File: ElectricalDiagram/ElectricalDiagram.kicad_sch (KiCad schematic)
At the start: 29 parts

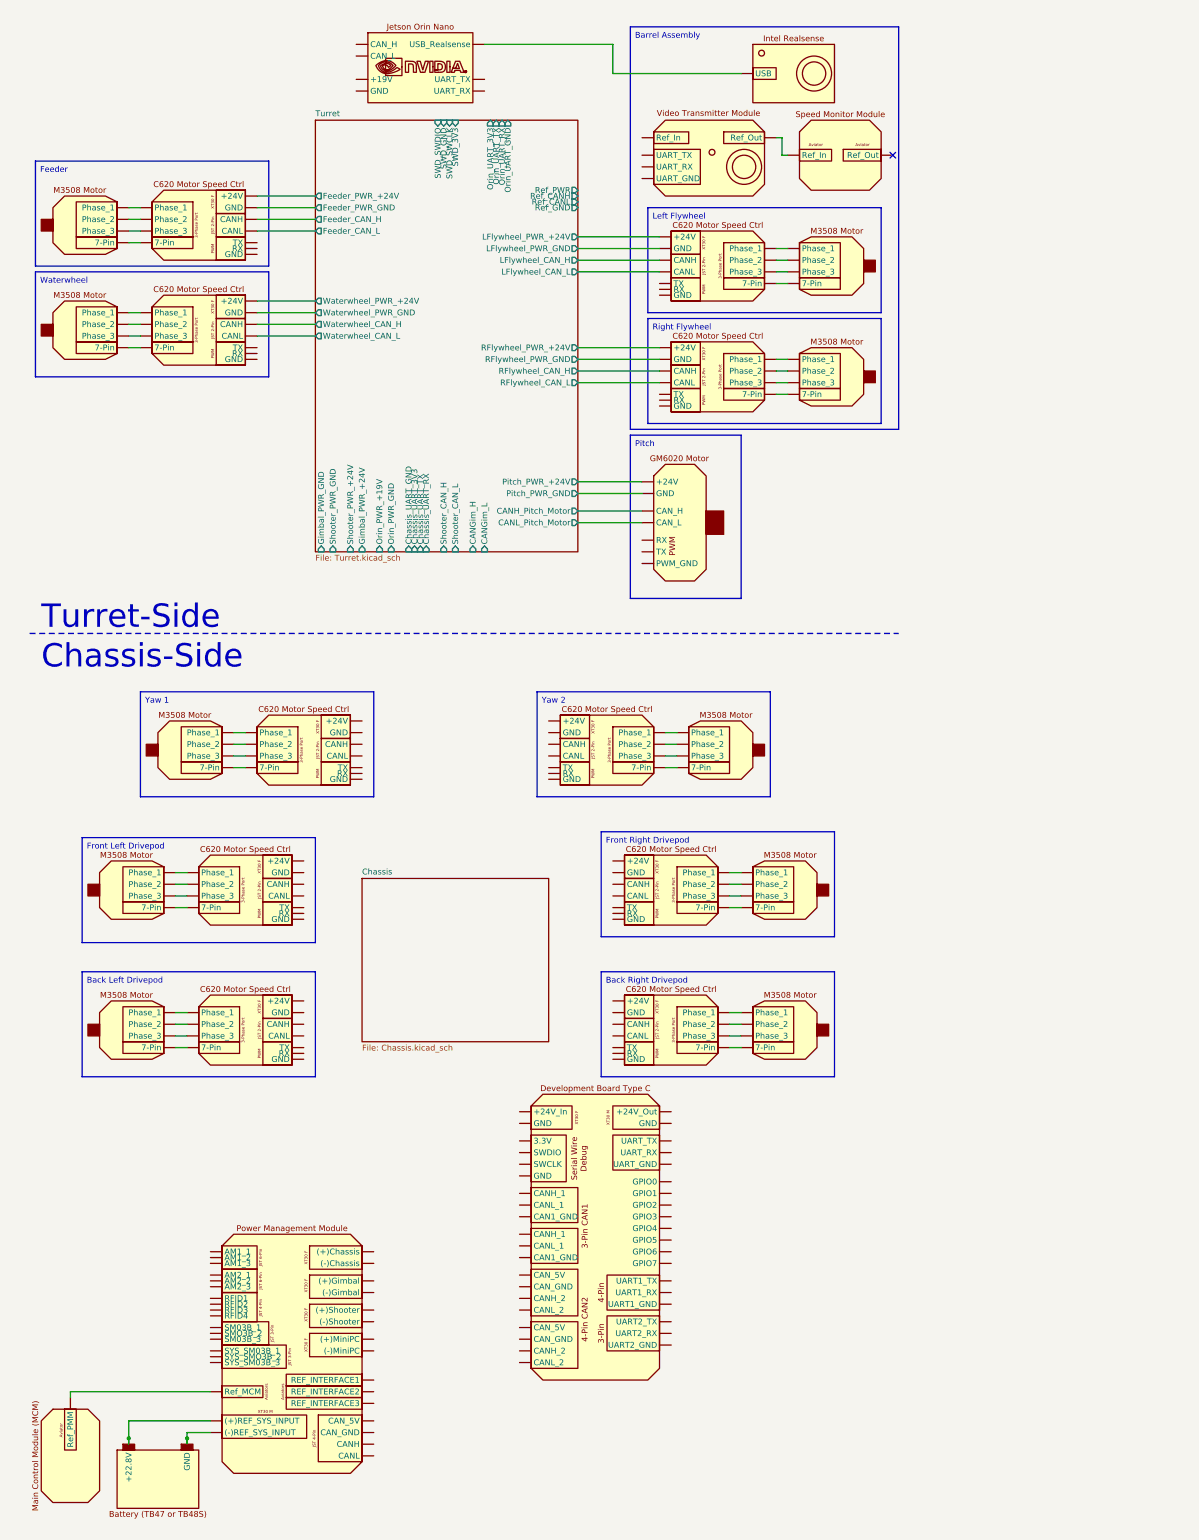
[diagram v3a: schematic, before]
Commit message: Staged hierarchical changes for chassis, not finished
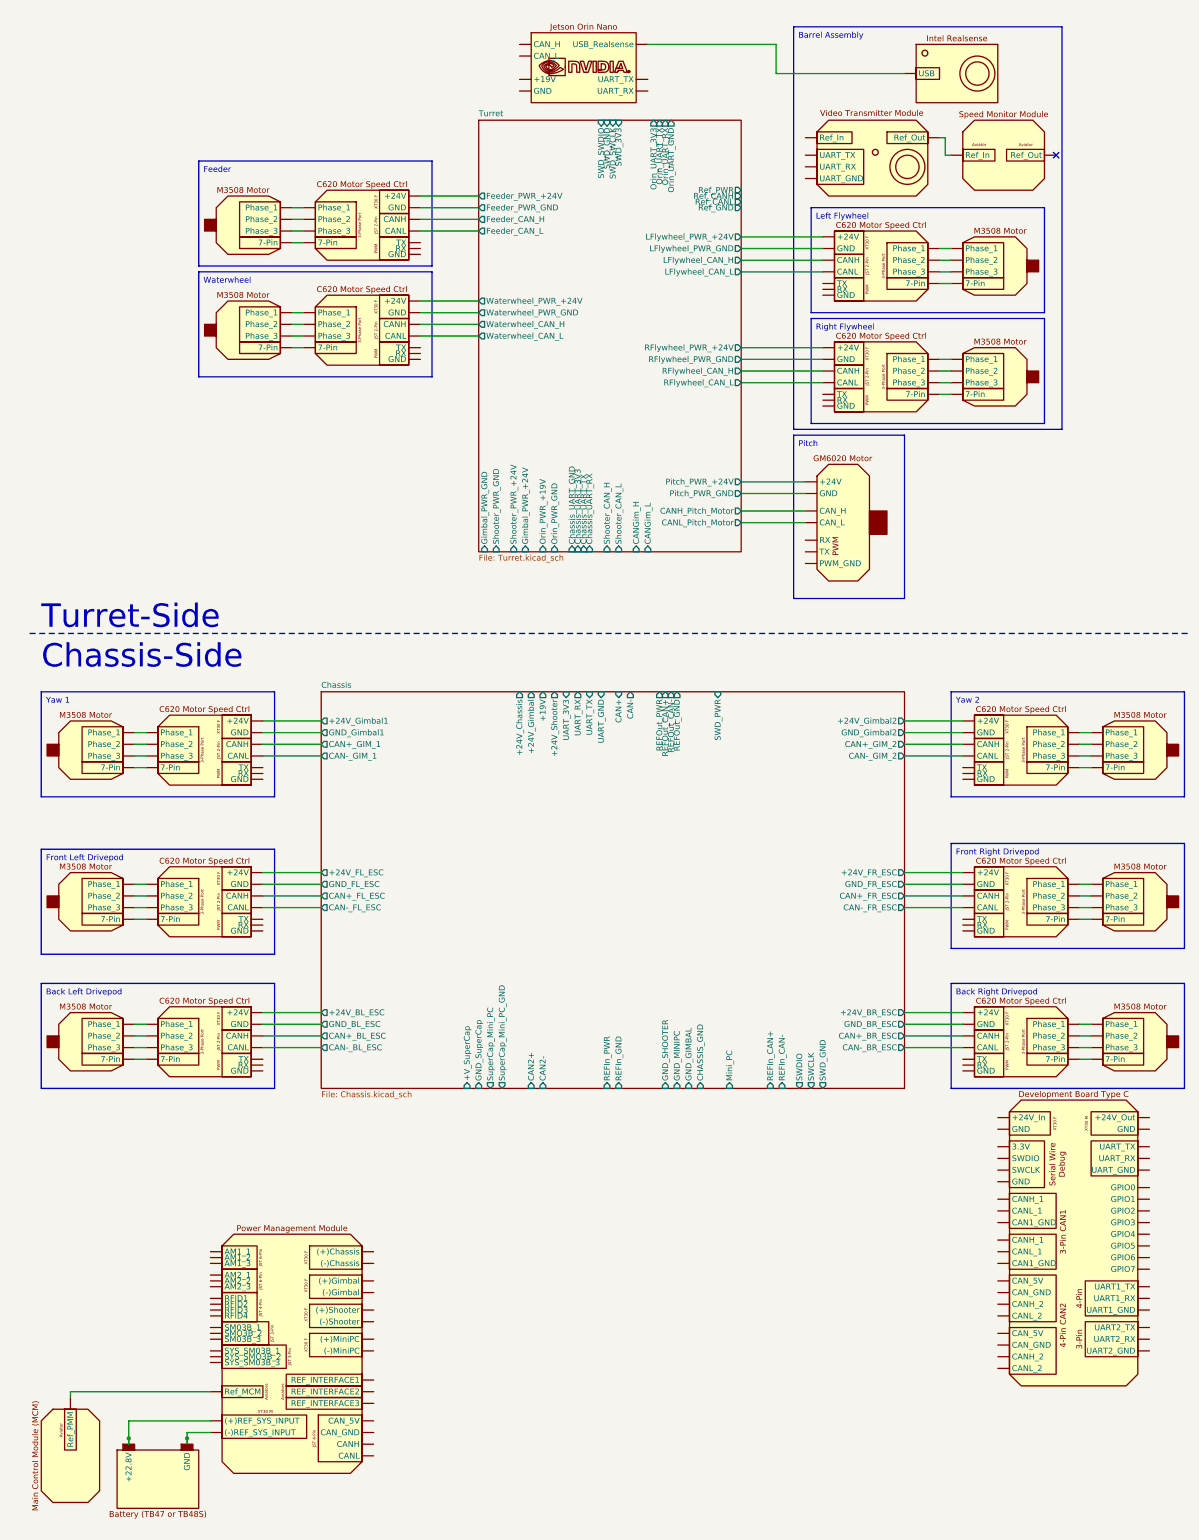
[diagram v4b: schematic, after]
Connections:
- net Chassis/GND_FL_ESC: now reaches U15. (TX)
- net Chassis/GND_Gimbal1: now reaches U25. (TX)
- net at U27. (SYS_SMO3B_2): no longer U28. (GND)
- net at U3. (UART_TX): now also U4. (Ref_Out)
- net at U4. (Ref_Out): no longer U3. (UART_TX)
- net Chassis/GND_Gimbal2: now reaches U23. (TX)
- net Chassis/GND_Gimbal2: no longer U22. (Phase_3)
- net Chassis/GND_BR_ESC: now reaches U21. (TX)
- net Chassis/GND_BR_ESC: no longer U20. (Phase_3)
- net Chassis/GND_BL_ESC: now reaches U17. (TX)
- net Chassis/GND_FR_ESC: now reaches U19. (TX)
- net Chassis/GND_FR_ESC: no longer U18. (Phase_3)
- new net: U10. (TX), U12. (Phase_3) (x3)
- new net: U5. (Phase_3), U7. (TX) (x3)
- new net: U11. (Phase_3), U13. (TX) (x3)
- new net: U14. (Phase_3), U15. (TX) (x3)
- new net: U24. (Phase_3), U25. (TX) (x3)
- new net: U27. (SYS_SMO3B_2), U28. (GND)
- new net: U8. (Phase_3), U9. (TX) (x3)
- new net: U22. (Phase_3), U23. (TX) (x3)
- new net: U20. (Phase_3), U21. (TX) (x3)
- new net: U16. (Phase_3), U17. (TX) (x3)
- new net: U18. (Phase_3), U19. (TX) (x3)
- new net Chassis/+24V_BL_ESC: U17. (TX)
- new net Chassis/+24V_BR_ESC: U21. (TX)
- new net Chassis/+24V_FL_ESC: U15. (TX)
- new net Chassis/+24V_FR_ESC: U19. (TX)
- new net Chassis/+24V_Gimbal1: U25. (TX)
- new net Chassis/+24V_Gimbal2: U23. (TX)
- new net Chassis/CAN+_BL_ESC: U17. (TX)
- new net Chassis/CAN+_BR_ESC: U21. (TX)
- new net Chassis/CAN+_FL_ESC: U15. (TX)
- new net Chassis/CAN+_FR_ESC: U19. (TX)
- new net Chassis/CAN+_GIM_1: U25. (TX)
- new net Chassis/CAN+_GIM_2: U23. (TX)
- new net Chassis/CAN-_BL_ESC: U17. (TX)
- new net Chassis/CAN-_BR_ESC: U21. (TX)
- new net Chassis/CAN-_FL_ESC: U15. (TX)
- new net Chassis/CAN-_FR_ESC: U19. (TX)
- new net Chassis/CAN-_GIM_1: U25. (TX)
- new net Chassis/CAN-_GIM_2: U23. (TX)
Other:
- sheet Chassis ports: added +19V, +24V_BL_ESC, +24V_BR_ESC, +24V_Chassis, +24V_FL_ESC, +24V_FR_ESC, +24V_Gimbal, +24V_Gimbal1, +24V_Gimbal2, +24V_Shooter, +V_SuperCap, CAN+, CAN+_BL_ESC, CAN+_BR_ESC, CAN+_FL_ESC, CAN+_FR_ESC, CAN+_GIM_1, CAN+_GIM_2, CAN-, CAN-_BL_ESC, CAN-_BR_ESC, CAN-_FL_ESC, CAN-_FR_ESC, CAN-_GIM_1, CAN-_GIM_2, CAN2+, CAN2-, CHASSIS_GND, GND_BL_ESC, GND_BR_ESC, GND_FL_ESC, GND_FR_ESC, GND_GIMBAL, GND_Gimbal1, GND_Gimbal2, GND_MINIPC, GND_SHOOTER, GND_SuperCap, Mini_PC, REFIn_CAN+, REFIn_CAN-, REFIn_GND, REFIn_PWR, REFOut_CAN+, REFOut_CAN-, REFOut_GND, REFOut_PWR, SWCLK, SWDIO, SWD_GND, SWD_PWR, SuperCap_Mini_PC, SuperCap_Mini_PC_GND, UART_3V3, UART_GND, UART_RX, UART_TX; removed none

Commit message: staging before meeting
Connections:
- net at U27. (SYS_SMO3B_2): no longer U28. (GND)
- net at U3. (UART_TX): now also U4. (Ref_Out)
- net at U4. (Ref_Out): no longer U3. (UART_TX)
- new net: U10. (TX), U12. (Phase_3) (x3)
- new net: U5. (Phase_3), U7. (TX) (x3)
- new net: U11. (Phase_3), U13. (TX) (x3)
- new net: U14. (Phase_3), U15. (TX) (x3)
- new net: U24. (Phase_3), U25. (TX) (x3)
- new net: U27. (SYS_SMO3B_2), U28. (GND)
- new net: U8. (Phase_3), U9. (TX) (x3)
- new net: U22. (Phase_3), U23. (TX) (x3)
- new net: U20. (Phase_3), U21. (TX) (x3)
- new net: U16. (Phase_3), U17. (TX) (x3)
- new net: U18. (Phase_3), U19. (TX) (x3)
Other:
- sheet Chassis ports: added +19V_GND, +24V_Chassis_GND, +24V_Gimbal_GND, +24V_Shooter_GND; removed none
